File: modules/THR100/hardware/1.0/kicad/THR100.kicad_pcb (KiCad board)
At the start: 2 copper layers, 75 x 75 mm, 50 parts, among them J1 CAN, J2 SWITCHES, J3 Screw_Terminal_01x02, J4 Screw_Terminal_01x02, K1 FINDER-32.21-x300, K2 FINDER-32.21-x300, Q1 NTE123A, Q2 NTE123A, SW1 SCR, SW2 MODE, SW3 INSTANCE, U1 MCP2551-I-P, U2 TMR-1-1211, U3 PDJR_Teensy_3.2, U4 CNY74-2H

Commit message: Rename module
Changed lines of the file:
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@@
   )
   (layers
-    (0 F.Cu signal)
-    (31 B.Cu signal)
-    (33 F.Adhes user)
-    (35 F.Paste user)
+    (0 F.Cu signal hide)
+    (31 B.Cu signal hide)
+    (33 F.Adhes user hide)
+    (35 F.Paste user hide)
     (37 F.SilkS user)
     (38 B.Mask user hide)
@@
     (43 Eco2.User user hide)
     (44 Edge.Cuts user)
-    (45 Margin user hide)
+    (45 Margin user)
     (46 B.CrtYd user)
     (47 F.CrtYd user)
@@
     (descr "Resistor, Axial_DIN0204 series, Axial, Vertical, pin pitch=2.54mm, 0.167W, length*diameter=3.6*1.6mm^2, http://cdn-reichelt.de/documents/datenblatt/B400/1_4W%23YAG.pdf")
     (tags "Resistor Axial_DIN0204 series Axial Vertical pin pitch 2.54mm 0.167W length 3.6mm diameter 1.6mm")
-    (fp_text reference R15 (at 1.27 -1.92 90) (layer F.SilkS)
+    (fp_text reference R15 (at 4.318 0 180) (layer F.SilkS)
       (effects (font (size 1 1) (thickness 0.15)))
     )
@@
     (descr "Resistor, Axial_DIN0204 series, Axial, Vertical, pin pitch=2.54mm, 0.167W, length*diameter=3.6*1.6mm^2, http://cdn-reichelt.de/documents/datenblatt/B400/1_4W%23YAG.pdf")
     (tags "Resistor Axial_DIN0204 series Axial Vertical pin pitch 2.54mm 0.167W length 3.6mm diameter 1.6mm")
-    (fp_text reference R14 (at 1.27 -1.92 90) (layer F.SilkS)
+    (fp_text reference R14 (at 4.318 0 180) (layer F.SilkS)
       (effects (font (size 1 1) (thickness 0.15)))
     )
@@
   (module PDJR:Phoenix-FK-MPT-2-3,5 (layer F.Cu)
     (at 166.04 157.48)
-    (fp_text reference J4 (at 0 2.5) (layer F.SilkS)
+    (fp_text reference J4 (at -9.398 -2.54) (layer F.SilkS)
       (effects (font (size 1 1) (thickness 0.15)))
     )
@@
   (module PDJR:Phoenix-FK-MPT-2-3,5 (layer F.Cu)
     (at 151.816 157.48)
-    (fp_text reference J3 (at 0 2.5) (layer F.SilkS)
+    (fp_text reference J3 (at -9.398 -2.54) (layer F.SilkS)
       (effects (font (size 1 1) (thickness 0.15)))
     )
@@
     (descr "Diode, DO-34_SOD68 series, Axial, Vertical, pin pitch=2.54mm, , length*diameter=3.04*1.6mm^2, , https://www.nxp.com/docs/en/data-sheet/KTY83_SER.pdf")
     (tags "Diode DO-34_SOD68 series Axial Vertical pin pitch 2.54mm  length 3.04mm diameter 1.6mm")
-    (fp_text reference D6 (at 1.27 -2.25566) (layer F.SilkS)
+    (fp_text reference D6 (at 2.794 1.778) (layer F.SilkS)
       (effects (font (size 1 1) (thickness 0.15)))
     )
@@
     (descr "Diode, DO-34_SOD68 series, Axial, Vertical, pin pitch=2.54mm, , length*diameter=3.04*1.6mm^2, , https://www.nxp.com/docs/en/data-sheet/KTY83_SER.pdf")
     (tags "Diode DO-34_SOD68 series Axial Vertical pin pitch 2.54mm  length 3.04mm diameter 1.6mm")
-    (fp_text reference D5 (at 1.27 -2.25566) (layer F.SilkS)
+    (fp_text reference D5 (at 2.794 1.778) (layer F.SilkS)
       (effects (font (size 1 1) (thickness 0.15)))
     )
@@
     (descr "Diode, DO-34_SOD68 series, Axial, Vertical, pin pitch=2.54mm, , length*diameter=3.04*1.6mm^2, , https://www.nxp.com/docs/en/data-sheet/KTY83_SER.pdf")
     (tags "Diode DO-34_SOD68 series Axial Vertical pin pitch 2.54mm  length 3.04mm diameter 1.6mm")
-    (fp_text reference D10 (at 1.27 -2.25566) (layer F.SilkS)
+    (fp_text reference D10 (at -0.508 -1.778) (layer F.SilkS)
       (effects (font (size 1 1) (thickness 0.15)))
     )
@@
     (descr "Diode, DO-34_SOD68 series, Axial, Vertical, pin pitch=2.54mm, , length*diameter=3.04*1.6mm^2, , https://www.nxp.com/docs/en/data-sheet/KTY83_SER.pdf")
     (tags "Diode DO-34_SOD68 series Axial Vertical pin pitch 2.54mm  length 3.04mm diameter 1.6mm")
-    (fp_text reference D9 (at 1.27 -2.25566) (layer F.SilkS)
+    (fp_text reference D9 (at -0.254 -1.778) (layer F.SilkS)
       (effects (font (size 1 1) (thickness 0.15)))
     )
@@
     (descr "Resistor, Axial_DIN0204 series, Axial, Horizontal, pin pitch=5.08mm, 0.167W, length*diameter=3.6*1.6mm^2, http://cdn-reichelt.de/documents/datenblatt/B400/1_4W%23YAG.pdf")
     (tags "Resistor Axial_DIN0204 series Axial Horizontal pin pitch 5.08mm 0.167W length 3.6mm diameter 1.6mm")
-    (fp_text reference R10 (at 2.54 -1.92 90) (layer F.SilkS)
+    (fp_text reference R10 (at 2.54 0 180) (layer F.SilkS)
       (effects (font (size 1 1) (thickness 0.15)))
     )
@@
     (descr "Resistor, Axial_DIN0204 series, Axial, Horizontal, pin pitch=5.08mm, 0.167W, length*diameter=3.6*1.6mm^2, http://cdn-reichelt.de/documents/datenblatt/B400/1_4W%23YAG.pdf")
     (tags "Resistor Axial_DIN0204 series Axial Horizontal pin pitch 5.08mm 0.167W length 3.6mm diameter 1.6mm")
-    (fp_text reference R8 (at 2.54 -1.92 90) (layer F.SilkS)
+    (fp_text reference R8 (at 2.794 -0.254 180) (layer F.SilkS)
       (effects (font (size 1 1) (thickness 0.15)))
     )
@@
     (descr "Resistor, Axial_DIN0204 series, Axial, Horizontal, pin pitch=5.08mm, 0.167W, length*diameter=3.6*1.6mm^2, http://cdn-reichelt.de/documents/datenblatt/B400/1_4W%23YAG.pdf")
     (tags "Resistor Axial_DIN0204 series Axial Horizontal pin pitch 5.08mm 0.167W length 3.6mm diameter 1.6mm")
-    (fp_text reference R6 (at 2.54 -1.92) (layer F.SilkS)
+    (fp_text reference R6 (at 2.794 0) (layer F.SilkS)
       (effects (font (size 1 1) (thickness 0.15)))
     )
@@
     (descr TO-18-3)
     (tags TO-18-3)
-    (fp_text reference Q1 (at 1.27 -4.02 90) (layer F.SilkS)
+    (fp_text reference Q1 (at 1.27 -2.032 180) (layer F.SilkS)
       (effects (font (size 1 1) (thickness 0.15)))
     )
@@
     (descr "Diode, DO-34_SOD68 series, Axial, Vertical, pin pitch=2.54mm, , length*diameter=3.04*1.6mm^2, , https://www.nxp.com/docs/en/data-sheet/KTY83_SER.pdf")
     (tags "Diode DO-34_SOD68 series Axial Vertical pin pitch 2.54mm  length 3.04mm diameter 1.6mm")
-    (fp_text reference D7 (at 1.27 -2.25566) (layer F.SilkS)
+    (fp_text reference D7 (at -2.032 -1.016) (layer F.SilkS)
       (effects (font (size 1 1) (thickness 0.15)))
     )
@@
     (descr "Through hole straight pin header, 1x02, 2.54mm pitch, single row")
     (tags "Through hole pin header THT 1x02 2.54mm single row")
-    (fp_text reference D3 (at 0 -2.33) (layer F.SilkS)
+    (fp_text reference D3 (at 1.016 -2.54) (layer F.SilkS)
       (effects (font (size 1 1) (thickness 0.15)))
     )
@@
     (descr "CP, Radial series, Radial, pin pitch=2.50mm, , diameter=5mm, Electrolytic Capacitor")
     (tags "CP Radial series Radial pin pitch 2.50mm  diameter 5mm Electrolytic Capacitor")
-    (fp_text reference C5 (at 1.25 -3.75 90) (layer F.SilkS)
+    (fp_text reference C5 (at 3.302 -3.302 180) (layer F.SilkS)
       (effects (font (size 1 1) (thickness 0.15)))
     )
@@
     (descr "Resistor, Axial_DIN0204 series, Axial, Horizontal, pin pitch=5.08mm, 0.167W, length*diameter=3.6*1.6mm^2, http://cdn-reichelt.de/documents/datenblatt/B400/1_4W%23YAG.pdf")
     (tags "Resistor Axial_DIN0204 series Axial Horizontal pin pitch 5.08mm 0.167W length 3.6mm diameter 1.6mm")
-    (fp_text reference R11 (at 2.54 -1.92 90) (layer F.SilkS)
+    (fp_text reference R11 (at 2.54 0.254 180) (layer F.SilkS)
       (effects (font (size 1 1) (thickness 0.15)))
     )
@@
     (descr "Resistor, Axial_DIN0204 series, Axial, Horizontal, pin pitch=5.08mm, 0.167W, length*diameter=3.6*1.6mm^2, http://cdn-reichelt.de/documents/datenblatt/B400/1_4W%23YAG.pdf")
     (tags "Resistor Axial_DIN0204 series Axial Horizontal pin pitch 5.08mm 0.167W length 3.6mm diameter 1.6mm")
-    (fp_text reference R9 (at 2.54 -1.92 90) (layer F.SilkS)
+    (fp_text reference R9 (at 2.794 0 180) (layer F.SilkS)
       (effects (font (size 1 1) (thickness 0.15)))
     )
@@
     (descr "Resistor, Axial_DIN0204 series, Axial, Horizontal, pin pitch=5.08mm, 0.167W, length*diameter=3.6*1.6mm^2, http://cdn-reichelt.de/documents/datenblatt/B400/1_4W%23YAG.pdf")
     (tags "Resistor Axial_DIN0204 series Axial Horizontal pin pitch 5.08mm 0.167W length 3.6mm diameter 1.6mm")
-    (fp_text reference R7 (at 2.54 -1.92) (layer F.SilkS)
+    (fp_text reference R7 (at 2.54 0) (layer F.SilkS)
       (effects (font (size 1 1) (thickness 0.15)))
     )
@@
     (descr TO-18-3)
     (tags TO-18-3)
-    (fp_text reference Q2 (at 1.27 -4.02 90) (layer F.SilkS)
+    (fp_text reference Q2 (at 1.27 -2.032 180) (layer F.SilkS)
       (effects (font (size 1 1) (thickness 0.15)))
     )
@@
     (descr "Diode, DO-34_SOD68 series, Axial, Vertical, pin pitch=2.54mm, , length*diameter=3.04*1.6mm^2, , https://www.nxp.com/docs/en/data-sheet/KTY83_SER.pdf")
     (tags "Diode DO-34_SOD68 series Axial Vertical pin pitch 2.54mm  length 3.04mm diameter 1.6mm")
-    (fp_text reference D8 (at 1.27 -2.25566) (layer F.SilkS)
+    (fp_text reference D8 (at -2.286 -1.016) (layer F.SilkS)
       (effects (font (size 1 1) (thickness 0.15)))
     )
@@
     (descr "Through hole straight pin header, 1x02, 2.54mm pitch, single row")
     (tags "Through hole pin header THT 1x02 2.54mm single row")
-    (fp_text reference D4 (at 0 -2.33) (layer F.SilkS)
+    (fp_text reference D4 (at 1.016 -2.54) (layer F.SilkS)
       (effects (font (size 1 1) (thickness 0.15)))
     )
@@
     (descr "CP, Radial series, Radial, pin pitch=2.50mm, , diameter=5mm, Electrolytic Capacitor")
     (tags "CP Radial series Radial pin pitch 2.50mm  diameter 5mm Electrolytic Capacitor")
-    (fp_text reference C6 (at 1.25 -3.75 90) (layer F.SilkS)
+    (fp_text reference C6 (at 3.302 -3.302 180) (layer F.SilkS)
       (effects (font (size 1 1) (thickness 0.15)))
     )
@@
     (descr "C, Rect series, Radial, pin pitch=2.50mm, , length*width=4.6*3.0mm^2, Capacitor, http://www.wima.de/DE/WIMA_MKS_02.pdf")
     (tags "C Rect series Radial pin pitch 2.50mm  length 4.6mm width 3.0mm Capacitor")
-    (fp_text reference C1 (at 3.008 -2.794 270) (layer F.SilkS)
-      (effects (font (size 1 1) (thickness 0.15)))
-    )
+    (fp_text reference C1 (at 3.048 -2.54) (layer F.SilkS)
+      (effects (font (size 1 1) (thickness 0.15)))
+    )

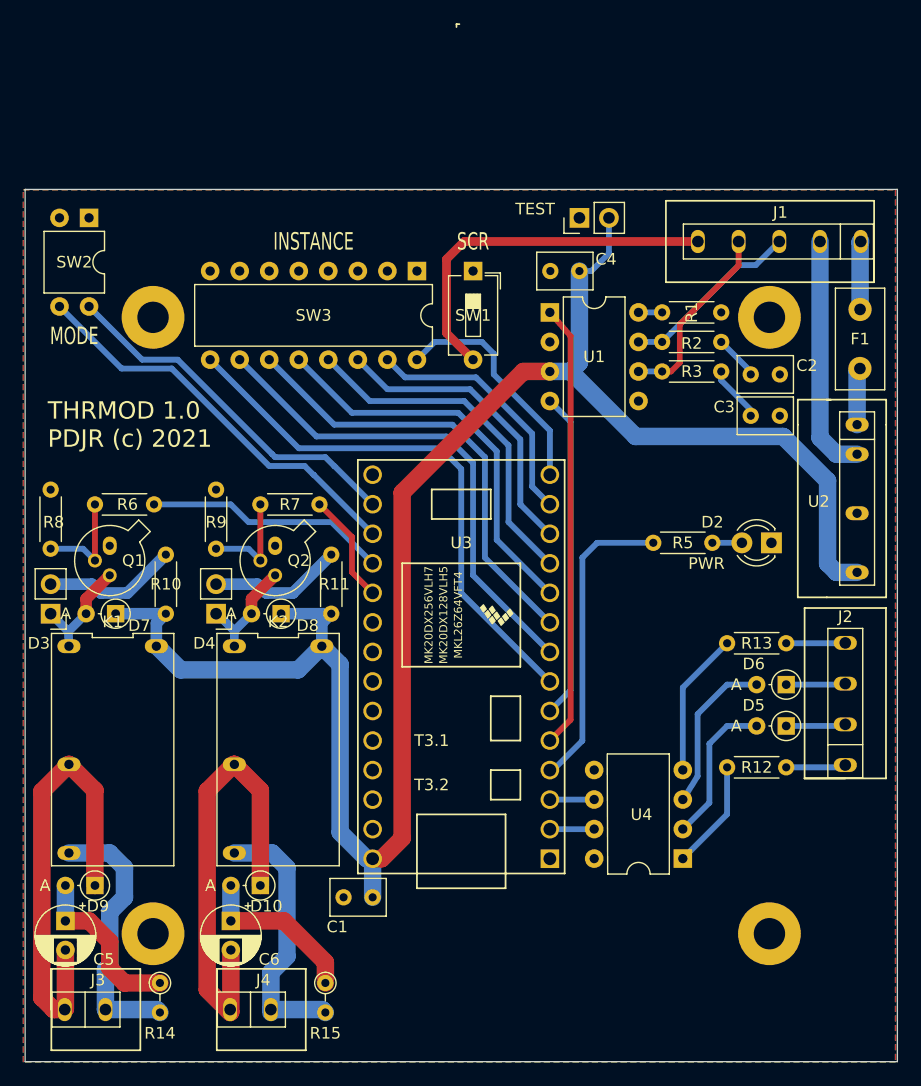
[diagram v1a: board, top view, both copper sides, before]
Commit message: Revised PCB for analog control
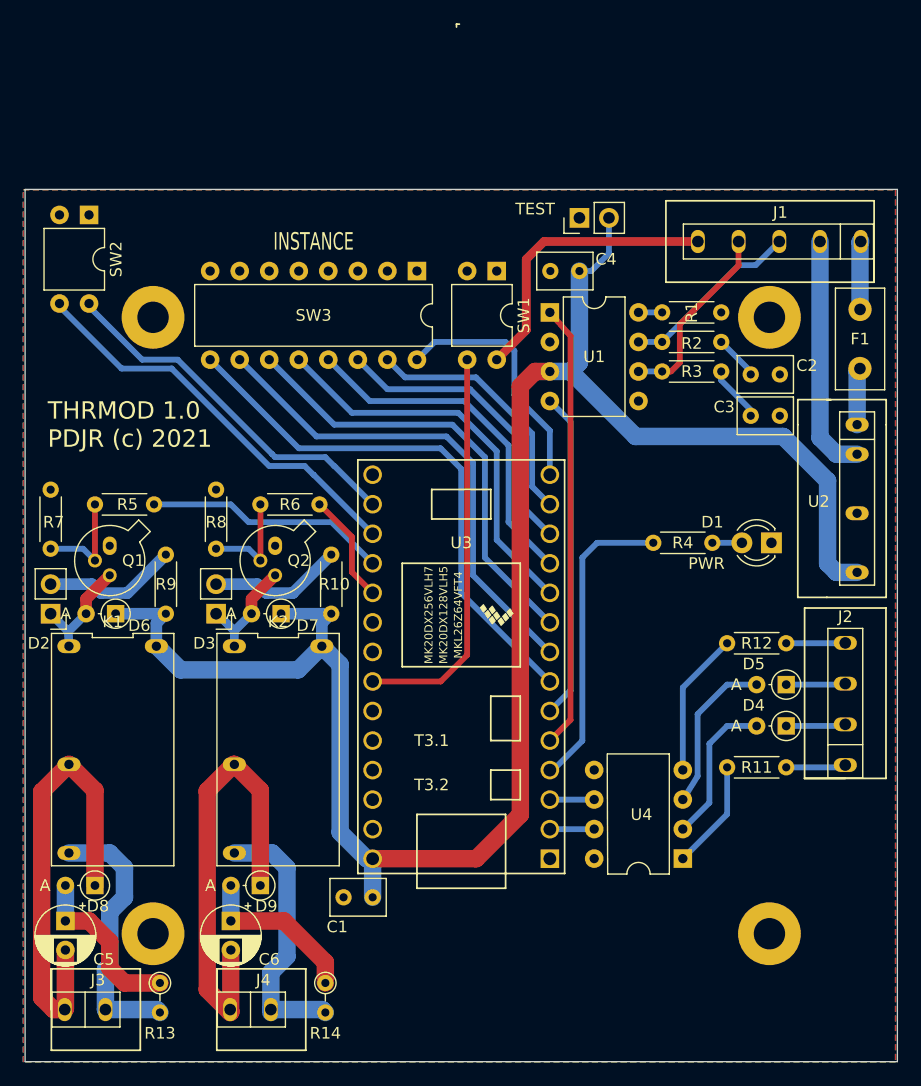
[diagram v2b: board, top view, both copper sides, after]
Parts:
- SW1: value SCR -> MODEA; footprint Button_Switch_THT:SW_DIP_SPSTx01_Slide_6.7x4.1mm_W7.62mm_P2.54mm_LowProfile -> Package_DIP:DIP-4_W7.62mm
- SW2: value MODE -> MODEB
- moved SW1 2.03 mm to (176.7, 94.0)
- moved SW2 0.25 mm to (141.7, 89.2)
- renumbered D2 to D1, D3 to D2, D4 to D3, D5 to D4, D6 to D5, D7 to D6, D8 to D7, D9 to D8, D10 to D9, R11 to R10, R12 to R11, R13 to R12, R14 to R13, R15 to R14, R5 to R4, R6 to R5, R7 to R6, R8 to R7, R9 to R8, R10 to R9
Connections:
- SW1 pad 2: /CAN_SCR -> Net-(SW1-Pad2)
- SW2 pad 1: GND -> Net-(SW1-Pad2)
- SW2 pad 2: GND -> Net-(SW2-Pad2)
- SW3 pad 1: GND -> Net-(SW2-Pad2)
- SW3 pad 2: GND -> Net-(SW2-Pad2)
- SW3 pad 3: GND -> Net-(SW2-Pad2)
- SW3 pad 4: GND -> Net-(SW2-Pad2)
- SW3 pad 5: GND -> Net-(SW2-Pad2)
- SW3 pad 6: GND -> Net-(SW2-Pad2)
- SW3 pad 7: GND -> Net-(SW2-Pad2)
- SW3 pad 8: GND -> Net-(SW2-Pad2)
- U3 pad 22: (no net) -> /ANALOG
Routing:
- net /ANALOG: track 0.00 -> 34.5 mm
- net /CAN_SCR: track 31.8 -> 25.1 mm
- net +5V: track 157.4 -> 161.6 mm
- net /ADDR_0: track 20.4 -> 21.6 mm

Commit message: Add proportianal hardware
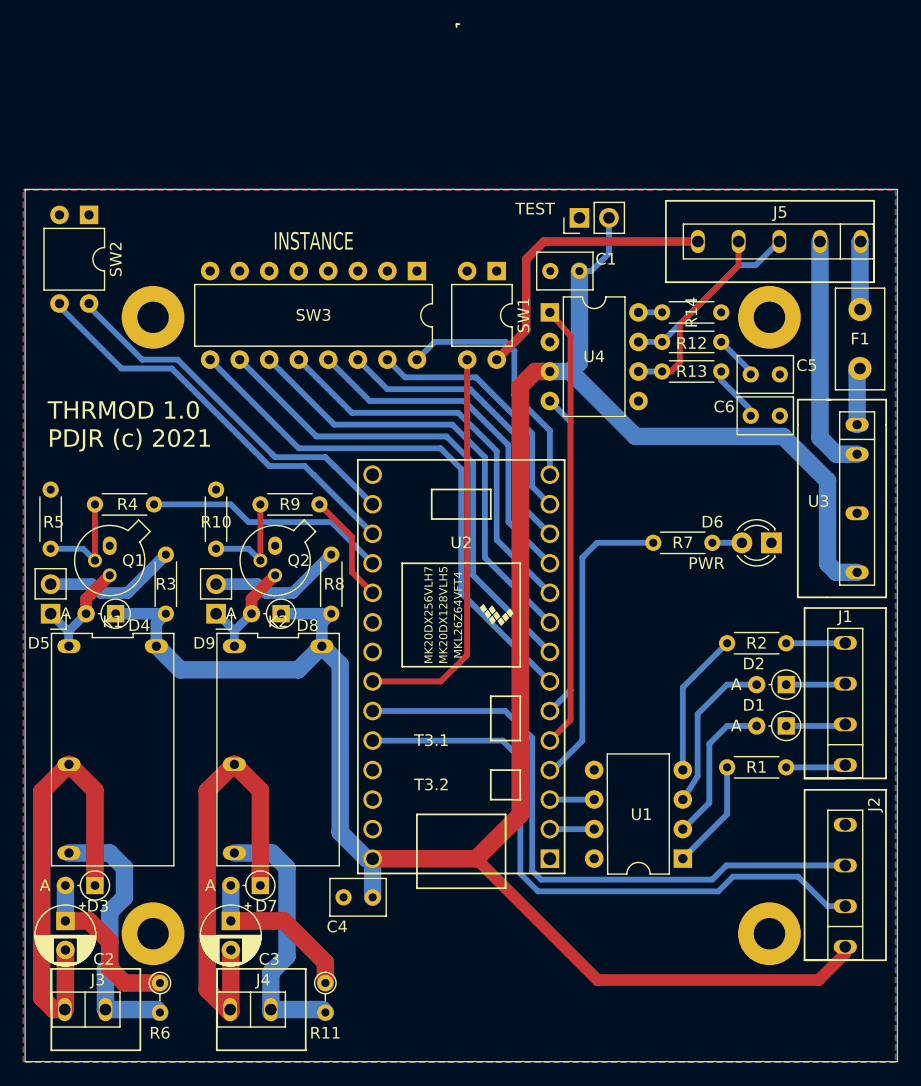
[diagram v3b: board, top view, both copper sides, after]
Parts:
- added J2: ANALOG_IN, PDJR:Phoenix-FK-MPT-4-3,5, F.Cu at (206.7, 139.8)
- renumbered C4 to C1, C5 to C2, C6 to C3, C1 to C4, C2 to C5, C3 to C6, D4 to D1, D5 to D2, D8 to D3, D6 to D4, D2 to D5, D1 to D6, D9 to D7, D7 to D8, D3 to D9, J2 to J1, J1 to J5, R11 to R1, R8 to R10, R14 to R11, R2 to R12, R3 to R13, R1 to R14, R12 to R2, R9 to R3, R5 to R4, R7 to R5, R13 to R6, R4 to R7, R10 to R8, R6 to R9, U4 to U1, U3 to U2, U2 to U3, U1 to U4
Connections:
- SW1 pad 2: Net-(SW1-Pad2) -> GND
- SW2 pad 1: Net-(SW1-Pad2) -> GND
- SW2 pad 2: Net-(SW2-Pad2) -> GND
- SW3 pad 1: Net-(SW2-Pad2) -> GND
- SW3 pad 2: Net-(SW2-Pad2) -> GND
- SW3 pad 3: Net-(SW2-Pad2) -> GND
- SW3 pad 4: Net-(SW2-Pad2) -> GND
- SW3 pad 5: Net-(SW2-Pad2) -> GND
- SW3 pad 6: Net-(SW2-Pad2) -> GND
- SW3 pad 7: Net-(SW2-Pad2) -> GND
- SW3 pad 8: Net-(SW2-Pad2) -> GND
- U2 pad 23: (no net) -> /PS_ADC
- U2 pad 24: (no net) -> /SB_ADC
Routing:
- net /PS_ADC: track 0.00 -> 53.8 mm
- net /SB_ADC: track 0.00 -> 53.4 mm
- net +5V: track 161.6 -> 199.2 mm

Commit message: PCB tweak
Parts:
- removed the U1 at (192.7, 144.5)
- removed the U2 at (173.7, 128.0)
- added U3: Teensy_3.2, Package_DIP:DIP-28_W15.24mm_Socket, F.Cu at (181.2, 144.5)
- added U4: CNY74-2H, Package_DIP:DIP-8_W7.62mm, F.Cu at (192.7, 144.5)
- SW1: value MODEA -> MISC
- SW2: value MODEB -> MODE
- moved C1 0.25 mm to (166.0, 148.1)
- renumbered C4 to C1, C5 to C2, C6 to C3, C1 to C4, C2 to C5, C3 to C6, D6 to D1, D5 to D2, D9 to D3, D1 to D4, D2 to D5, D4 to D6, D8 to D7, D3 to D8, D7 to D9, J5 to J1, J1 to J2, J2 to J3, J3 to J4, J4 to J5, R14 to R1, R8 to R10, R1 to R11, R2 to R12, R6 to R13, R11 to R14, R12 to R2, R13 to R3, R7 to R4, R4 to R5, R9 to R6, R5 to R7, R10 to R8, R3 to R9, U4 to U1, U3 to U2
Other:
- board text added: "COMMON"
- board text added: "MODE"
- board text added: "PROP"
- board text added: "SCR"
